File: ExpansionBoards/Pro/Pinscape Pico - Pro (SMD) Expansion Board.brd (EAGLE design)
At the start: 170.6 x 108 mm, 179 parts, among them IC1 UCC27523D, IC10 UCC27523D, IC11 UCC27523D, IC12 UCC27523D, IC13 UCC27523D, IC14 UCC27523D, IC15 TLC59116FIRHBR, IC16 TLC59116FIRHBR, IC17 TLC59116FIRHBR, IC18 TLC59116FIRHBR, IC19 ULN2803ADWR, IC2 UCC27523D, IC20 ULN2803ADWR, IC21 ULN2803ADWR, IC22 ULN2803ADWR, IC23 ULN2803ADWR, IC24 PCA9555APW,118, IC25 PCA9555APW,118, IC26 LIS3DHTR, IC27 SN74LVC1G175DCKR, IC28 APX809S-29SA-7, IC29 LTV-827S, IC3 UCC27523D, IC30 ADS1115IDGSR, IC31 TLV75733PDBVR, IC33 RV-3032-C7, IC4 UCC27523D, IC5 UCC27523D, IC6 UCC27523D, IC7 UCC27523D, IC8 UCC27523D, IC9 UCC27523D, J1 640445-4, J10 1-640456-0, J11 1-640456-0, J12 1-640456-0, J13 640445-5, J14 640445-9, J15 640445-9, J16 640445-9, J18 BM03B-SRSS-TB(LF)(SN), J2 30316-6002HB, J3 1-640456-0, J4 640456-9, J5 640456-9, J6 640454-2, J7 215079-4, J8 30308-6002HB, J9 1-640456-0, Q1 BUK7K89-100EX, Q10 BUK7K89-100EX, Q11 BUK7K89-100EX, Q12 BUK7K89-100EX, Q13 BUK7K89-100EX, Q14 BUK7K89-100EX, Q15 UMA5NTR, Q16 UMA5NTR, Q17 UMA5NTR, Q18 UMA5NTR, Q19 UMA5NTR, Q2 BUK7K89-100EX, Q20 UMA5NTR, Q21 UMA5NTR, Q22 UMA5NTR, Q23 UMA5NTR, Q24 UMA5NTR, Q25 UMA5NTR, Q26 UMA5NTR, Q29 DMG2302UK-7, Q3 BUK7K89-100EX, Q4 BUK7K89-100EX, Q5 BUK7K89-100EX, Q6 BUK7K89-100EX, Q7 BUK7K89-100EX, Q8 BUK7K89-100EX, Q9 BUK7K89-100EX, SW1 TS-1187A-B-A-B, U1 BAT-HLD-001-THM

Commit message: bug fixes
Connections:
- net 3V3_PERIPHERAL: now also IC26.8
- net GND: now also IC26.7; no longer IC26.8
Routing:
- net 3V3_PERIPHERAL: track 399.6 -> 404.9 mm, vias 17 -> 18
- net GND: track 105.4 -> 103.7 mm

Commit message: expansion board improvements
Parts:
- J1: value 640445-4 -> 640445-6; device SamacSys_Parts:SHDR4W117P0X396_1X4_1585X762X1 -> SamacSys_Parts:SHDR6W183P0X396_1X6_2377X762X1
- moved J1 8.71 mm to (157.3, 95.1), turned to 270 degrees
- moved R20 2.10 mm to (97.5, 83.1), turned to 270 degrees
- moved R24 2.06 mm to (114.9, 83.1), turned to 270 degrees
- moved R28 2.06 mm to (132.3, 83.1), turned to 270 degrees
- moved R12 2.06 mm to (62.6, 83.1), turned to 270 degrees
- moved R14 2.06 mm to (71.3, 83.1), turned to 270 degrees
- moved R16 2.06 mm to (80.0, 83.1), turned to 270 degrees
- moved R18 2.06 mm to (88.7, 83.1), turned to 270 degrees
- moved R22 2.06 mm to (106.1, 83.1), turned to 270 degrees
- moved R26 2.02 mm to (123.4, 83.1), turned to 270 degrees
- moved R10 2.02 mm to (53.9, 83.1), turned to 270 degrees
- moved R4 2.01 mm to (24.6, 83.1), turned to 270 degrees
- moved R8 1.99 mm to (45.2, 83.1), turned to 270 degrees
- moved R2 1.97 mm to (15.8, 83.1), turned to 270 degrees
- moved R6 1.97 mm to (36.8, 83.1), turned to 270 degrees
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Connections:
- net 12V: now also J1.5; no longer J1.4
- net 5V: now also J1.6; no longer J1.1
- net GND: now also J1.1, J1.4
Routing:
- net 5V: track 359.3 -> 341.6 mm
- net 12V: track 295.6 -> 290.5 mm
- net N$19: track 5.34 -> 2.07 mm
- net N$9: track 5.30 -> 2.03 mm
- net N$4: track 5.34 -> 2.07 mm
- net N$27: track 5.30 -> 2.03 mm
- net N$16: track 5.34 -> 2.07 mm
- net N$18: track 5.30 -> 2.07 mm
- net N$24: track 5.30 -> 2.07 mm
- net N$11: track 5.30 -> 2.07 mm
- net N$6: track 5.37 -> 2.15 mm
- net N$3: track 5.34 -> 2.14 mm
- net N$33: track 5.20 -> 2.03 mm
- net N$21: track 5.24 -> 2.11 mm
- net N$61: track 5.16 -> 2.03 mm
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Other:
- board text added: "2ND PSU"
- board text added: "REV 20250106"
- board text removed: "REV 20241208"

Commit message: add logo image
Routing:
- net GND: track 103.0 -> 116.7 mm
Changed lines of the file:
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@@
 <via x="138" y="22.9" extent="1-16" drill="0.5"/>
 <via x="138.7" y="9.4" extent="1-16" drill="0.5"/>
-<polygon width="0.2" layer="1" thermals="no">
-<vertex x="155.1" y="92.9"/>
-<vertex x="159.4" y="92.9"/>
-<vertex x="159.4" y="77.3"/>
-<vertex x="155.1" y="77.3"/>
-</polygon>
-<polygon width="0.2" layer="16" thermals="no">
-<vertex x="155" y="92.9"/>
-<vertex x="159.3" y="92.9"/>
-<vertex x="159.3" y="77.3"/>
-<vertex x="155" y="77.3"/>
-</polygon>
 <contactref element="J1" pad="1"/>
+<wire x1="157.3" y1="91.14" x2="155.64" y2="91.14" width="1.5" layer="16"/>
+<wire x1="157.3" y1="87.18" x2="155.78" y2="87.18" width="1.5" layer="16"/>
+<wire x1="157.3" y1="83.22" x2="155.72" y2="83.22" width="1.5" layer="16"/>
+<wire x1="157.3" y1="95.1" x2="155.3" y2="95.1" width="1.5" layer="16"/>
+<wire x1="157.3" y1="95.1" x2="155.3" y2="95.1" width="1.5" layer="1"/>
+<wire x1="157.3" y1="91.14" x2="155.54" y2="91.14" width="1.5" layer="1"/>
+<wire x1="157.3" y1="87.18" x2="155.72" y2="87.18" width="1.5" layer="1"/>
+<wire x1="157.3" y1="83.22" x2="155.62" y2="83.22" width="1.5" layer="1"/>
 </signal>
 <signal name="5V">

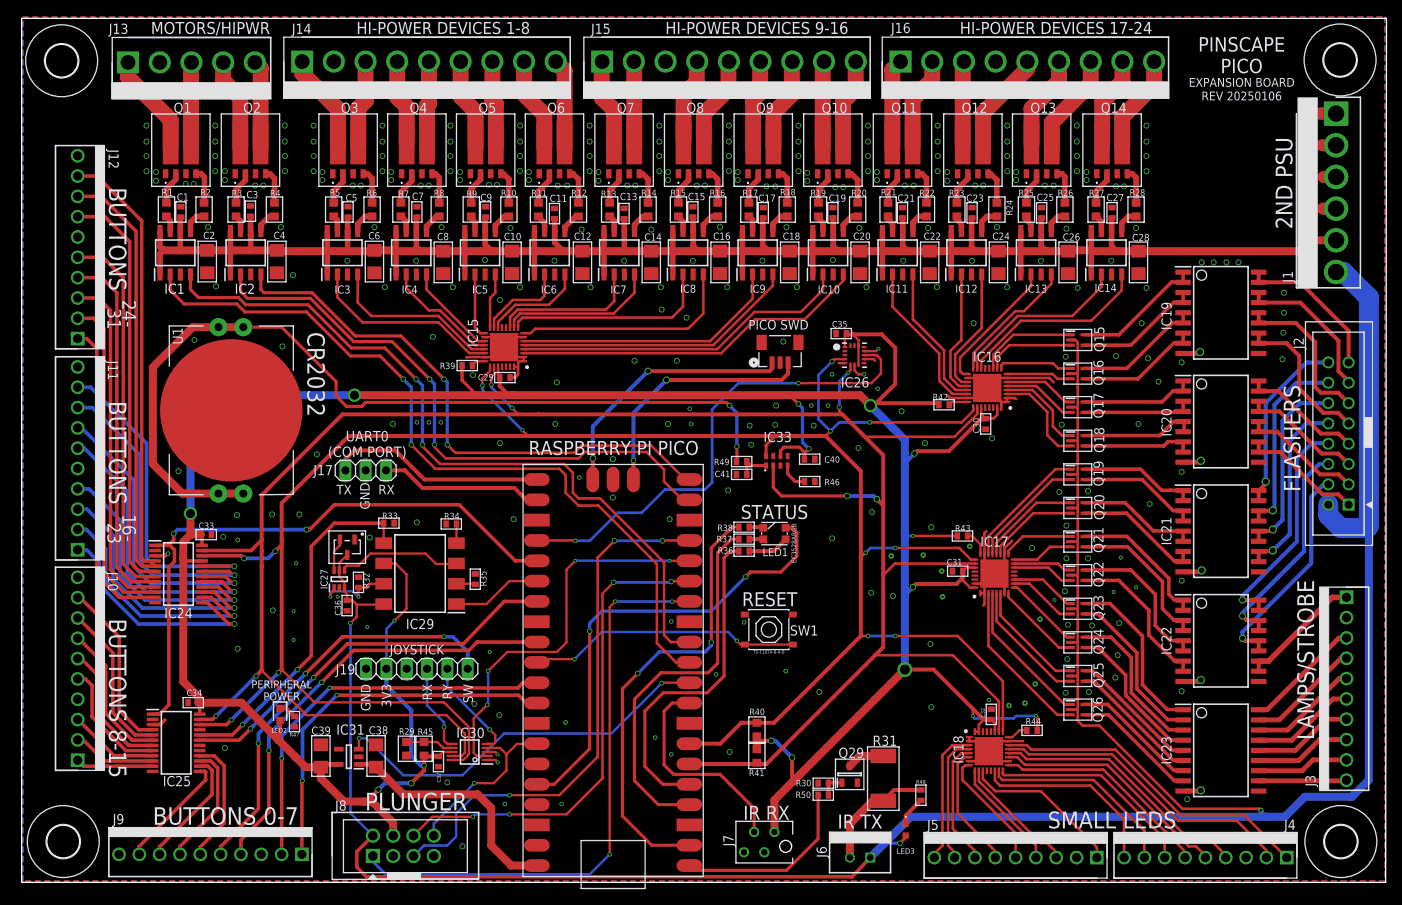
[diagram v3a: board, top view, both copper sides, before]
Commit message: Update Pro expansion board to use 74HC165 for all button inputs
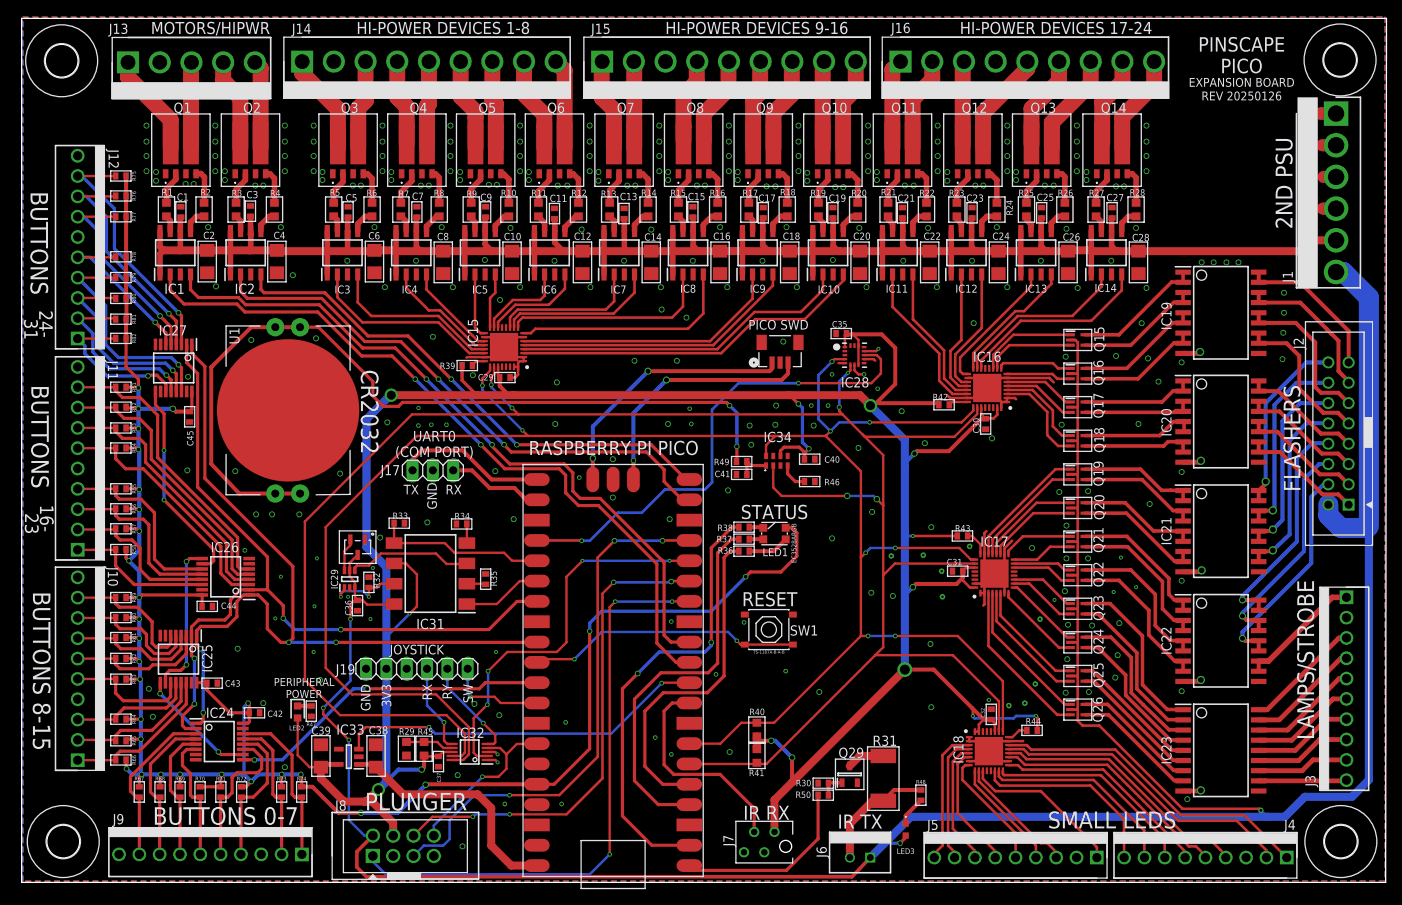
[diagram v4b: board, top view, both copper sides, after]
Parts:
- removed C33, C34: 0.1uF, rcl:C0402
- added C42, C43, C44, C45: 0.1uF, rcl:C0402
- added IC32: ADS1115IDGSR, SamacSys_Parts:SOP50P490X110-10N
- added IC34: RV-3032-C7, SamacSys_Parts:RV3032C7
- added R51, R52, R53, R54, R55, R56, R57, R58, R59, R60, R61, R62, R63, R64, R65, R66, R67, R68, R69, R70, R71, R72, R73, R74, R75, R76, R77, R78, R79, R80, R81, R82: 10k, resistor:R0402
- IC24, IC25: value PCA9555APW,118 -> SN74HC165PWR; device SamacSys_Parts:SOP65P640X110-24N -> SamacSys_Parts:SOP65P640X120-16N
- IC26: value LIS3DHTR -> SN74HC165PWR; device SamacSys_Parts:LIS3DHTR -> SamacSys_Parts:SOP65P640X120-16N
- IC27: value SN74LVC1G175DCKR -> SN74HC165PWR; device SamacSys_Parts:SOP65P210X110-6N -> SamacSys_Parts:SOP65P640X120-16N
- IC28: value APX809S-29SA-7 -> LIS3DHTR; device SamacSys_Parts:SOT23_DIO -> SamacSys_Parts:LIS3DHTR
- IC29: value LTV-827S -> SN74LVC1G175DCKR; device SamacSys_Parts:SOP254P1016X460-8N -> SamacSys_Parts:SOP65P210X110-6N
- IC30: value ADS1115IDGSR -> APX809S-29SA-7; device SamacSys_Parts:SOP50P490X110-10N -> SamacSys_Parts:SOT23_DIO
- IC31: value TLV75733PDBVR -> LTV-827S; device SamacSys_Parts:SOT95P280X145-5N -> SamacSys_Parts:SOP254P1016X460-8N
- IC33: value RV-3032-C7 -> TLV75733PDBVR; device SamacSys_Parts:RV3032C7 -> SamacSys_Parts:SOT95P280X145-5N
- moved IC26 83.3 mm to (18.5, 37.2), turned to 180 degrees
- moved IC28 67.8 mm to (97.1, 64.9), turned to 0 degrees
- moved IC33 65.0 mm to (33.9, 14.7), turned to 180 degrees
- moved IC27 33.5 mm to (12.0, 63.3), turned to 270 degrees
- moved IC30 29.2 mm to (35.0, 40.9)
- moved IC31 25.1 mm to (44.1, 37.6)
- moved IC24 21.6 mm to (17.7, 16.6)
- moved IC25 10.5 mm to (12.6, 26.9), turned to 270 degrees
- moved IC29 8.83 mm to (34.0, 36.9), turned to 90 degrees
- moved J17 8.40 mm to (44.4, 50.5)
- moved U1 7.10 mm to (26.3, 58.0)
- moved R47 2.47 mm to (29.2, 20.4)
- moved LED2 2.22 mm to (27.5, 20.3)
- moved R33 1.30 mm to (40.2, 43.9)
- moved C36 1.30 mm to (35.0, 33.6)
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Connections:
- removed net BUTTON_INTR: IC24.1, IC25.1, PICO1.GP19
- removed net FLIPPER_BTN_1: J9.1, PICO1.GP27_A1
- removed net FLIPPER_BTN_2: J9.2, PICO1.GP26_A0
- removed net FLIPPER_BTN_3: J9.4, PICO1.GP22
- removed net FLIPPER_BTN_4: J9.5, PICO1.GP21
- new net BUTTON1: IC24.14, J9.1, R74.2
- new net BUTTON2: IC24.13, J9.2, R73.2
- new net BUTTON3: IC24.12, J9.4, R72.2
- new net BUTTON32: IC27.3, J12.9, R75.2
- new net BUTTON_CLK: IC24.2, IC25.2, IC26.2, IC27.2, PICO1.GP21
- new net BUTTON_DATA: IC24.9, PICO1.GP26_A0
- new net BUTTON_SHLD: IC24.1, IC25.1, IC26.1, IC27.1, PICO1.GP22
- new net N$78: IC25.10, IC26.9
- new net N$79: IC24.10, IC25.9
- new net N$80: IC26.10, IC27.9
- net 3V3_PERIPHERAL: now also IC28.1, IC28.14, IC28.8, IC31.6, IC32.8, IC33.5, IC34.6; no longer C33.1, C34.1, IC24.21, IC24.24, IC25.24, IC26.1, IC26.14, IC26.8, IC29.6, IC30.8, IC31.5, IC33.6
- net 3V3_PERIPHERAL_ENABLE: now also IC33.3; no longer IC31.3
- net 3V3_PICO: now also C42.1, C43.1, C44.1, C45.1, IC24.16, IC25.16, IC26.16, IC27.16, R51.1, R52.1, R53.1, R54.1, R55.1, R56.1, R57.1, R58.1, R59.1, R60.1, R61.1, R62.1, R63.1, R64.1, R65.1, R66.1, R67.1, R68.1, R69.1, R70.1, R71.1, R72.1, R73.1, R74.1, R75.1, R76.1, R77.1, R78.1, R79.1, R80.1, R81.1, R82.1
- net 5V: now also IC29.3, IC29.5, IC30.3, IC31.8; no longer IC27.3, IC27.5, IC28.3, IC29.8
- net ACCEL_INTR: now also IC28.11; no longer IC26.11
- net ADC_INTR: now also IC32.2; no longer IC30.2
- net BUTTON10: now also IC25.13, J10.2, R65.2; no longer IC25.9, J10.3
- net BUTTON11: now also IC25.12, J10.3, R64.2; no longer IC25.8, J10.5
- net BUTTON12: now also IC25.11, J10.5, R63.2; no longer IC25.7, J10.6
- net BUTTON13: now also IC25.3, J10.6, R62.2; no longer IC25.6, J10.7
- net BUTTON14: now also IC25.4, J10.7, R61.2; no longer IC25.5, J10.8
- net BUTTON15: now also IC25.5, J10.8, R60.2; no longer IC25.4, J10.9
- net BUTTON16: now also IC25.6, J10.9, R59.2; no longer IC24.13, J11.1
- net BUTTON17: now also IC26.14, J11.1, R58.2; no longer IC24.14, J11.2
- net BUTTON18: now also IC26.13, J11.2, R57.2; no longer IC24.15, J11.3
- net BUTTON19: now also IC26.12, J11.3, R56.2; no longer IC24.16, J11.4
- net BUTTON20: now also IC26.11, J11.4, R55.2; no longer IC24.17, J11.6
- net BUTTON21: now also IC26.3, J11.6, R54.2; no longer IC24.18, J11.7
- net BUTTON22: now also IC26.4, J11.7, R53.2; no longer IC24.19, J11.8
- net BUTTON23: now also IC26.5, J11.8, R52.2; no longer IC24.20, J11.9
- net BUTTON24: now also IC26.6, J11.9, R51.2; no longer IC24.11, J12.1
- net BUTTON25: now also IC27.11, J12.1, R82.2; no longer IC24.10, J12.2
- net BUTTON26: now also IC27.12, J12.2, R81.2; no longer IC24.9, J12.3
- net BUTTON27: now also IC27.13, J12.3, R80.2; no longer IC24.8, J12.4
- net BUTTON28: now also IC27.14, J12.4, R79.2; no longer IC24.7, J12.5
- net BUTTON29: now also IC27.6, J12.5, R78.2; no longer IC24.6, J12.7
- net BUTTON30: now also IC27.5, J12.7, R77.2; no longer IC24.5, J12.8
- net BUTTON31: now also IC27.4, J12.8, R76.2; no longer IC24.4, J12.9
- net BUTTON4: now also IC24.11, J9.5, R71.2; no longer IC25.16, J9.6
- net BUTTON5: now also IC24.6, J9.6, R70.2; no longer IC25.15, J9.7
- net BUTTON6: now also IC24.5, J9.7, R69.2; no longer IC25.14, J9.8
- net BUTTON7: now also IC24.4, J9.8, R68.2; no longer IC25.13, J9.9
- net BUTTON8: now also IC24.3, J9.9, R67.2; no longer IC25.11, J10.1
- net BUTTON9: now also IC25.14, J10.1, R66.2; no longer IC25.10, J10.2
- net GND: now also C42.2, C43.2, C44.2, C45.2, IC24.15, IC24.8, IC25.15, IC25.8, IC26.15, IC26.8, IC27.15, IC27.8, IC28.10, IC28.12, IC28.5, IC28.7, IC29.2, IC32.1, IC32.3, IC33.2, IC34.5; no longer C33.2, C34.2, IC24.12, IC24.2, IC24.3, IC25.12, IC25.2, IC25.21, IC25.3, IC26.10, IC26.12, IC26.5, IC26.7, IC27.2, IC28.1, IC30.3, IC31.2, IC33.5
- net JOYSTICK_BUTTON: now also PICO1.GP27_A1; no longer IC25.19
- net JOYSTICK_X: now also IC32.6; no longer IC30.6
- net JOYSTICK_Y: now also IC32.5; no longer IC30.5
- net N$58: now also IC29.1, IC31.7; no longer IC27.1, IC29.7
- net N$59: now also IC31.2; no longer IC29.2
- net N$63: now also IC29.6, IC30.2; no longer IC27.6, IC28.2
- net N$65: now also IC31.4; no longer IC29.4
- net N$68: now also IC29.4, IC31.3; no longer IC27.4, IC29.3
- net N$71: now also IC32.7; no longer IC30.7
- net N$73: now also IC34.4; no longer IC33.4
- net N$76: now also IC34.1; no longer IC33.1
- net PLUNGER_ADC: now also IC32.4; no longer IC30.4
- net PSU2_STATUS_SENSE: now also IC31.5, PICO1.GP19; no longer IC25.20, IC29.5
- net PSU2_STATUS_SET: now also IC31.1; no longer IC29.1
- net SCL: now also IC28.4, IC32.10, IC34.8; no longer IC24.22, IC25.22, IC26.4, IC30.10, IC33.8
- net SDA: now also IC28.6, IC32.9, IC34.2; no longer IC24.23, IC25.23, IC26.6, IC30.9, IC33.2
- net VBUS: now also IC33.1; no longer IC31.1
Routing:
- net 3V3_PICO: track 58.1 -> 269.8 mm, vias 2 -> 29
- net BUTTON_SHLD: track 0.00 -> 105.1 mm, vias 0 -> 4
- net BUTTON_CLK: track 0.00 -> 100.4 mm, vias 0 -> 4
- net BUTTON_INTR: track 76.4 -> 0.00 mm, vias 2 -> 0
- net FLIPPER_BTN_4: track 58.8 -> 0.00 mm, vias 2 -> 0
- net FLIPPER_BTN_3: track 54.7 -> 0.00 mm, vias 2 -> 0
- net FLIPPER_BTN_2: track 49.5 -> 0.00 mm, vias 2 -> 0
- net FLIPPER_BTN_1: track 47.1 -> 0.00 mm, vias 2 -> 0
- net 3V3_PERIPHERAL: track 403.3 -> 359.3 mm, vias 17 -> 15
- net SCL: track 294.8 -> 253.6 mm, vias 13 -> 9
- net BUTTON_DATA: track 0.00 -> 40.8 mm, vias 0 -> 2
- net SDA: track 298.7 -> 263.2 mm, vias 8 -> 6
- net BUTTON32: track 0.00 -> 31.5 mm, vias 0 -> 1
- net BUTTON29: track 51.5 -> 21.2 mm, vias 0 -> 1
- net JOYSTICK_BUTTON: track 41.8 -> 12.3 mm, vias 3 -> 1
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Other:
- board text added: "REV 20250126"
- board text removed: "REV 20250106"

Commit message: change to socketed Pico for Pro board
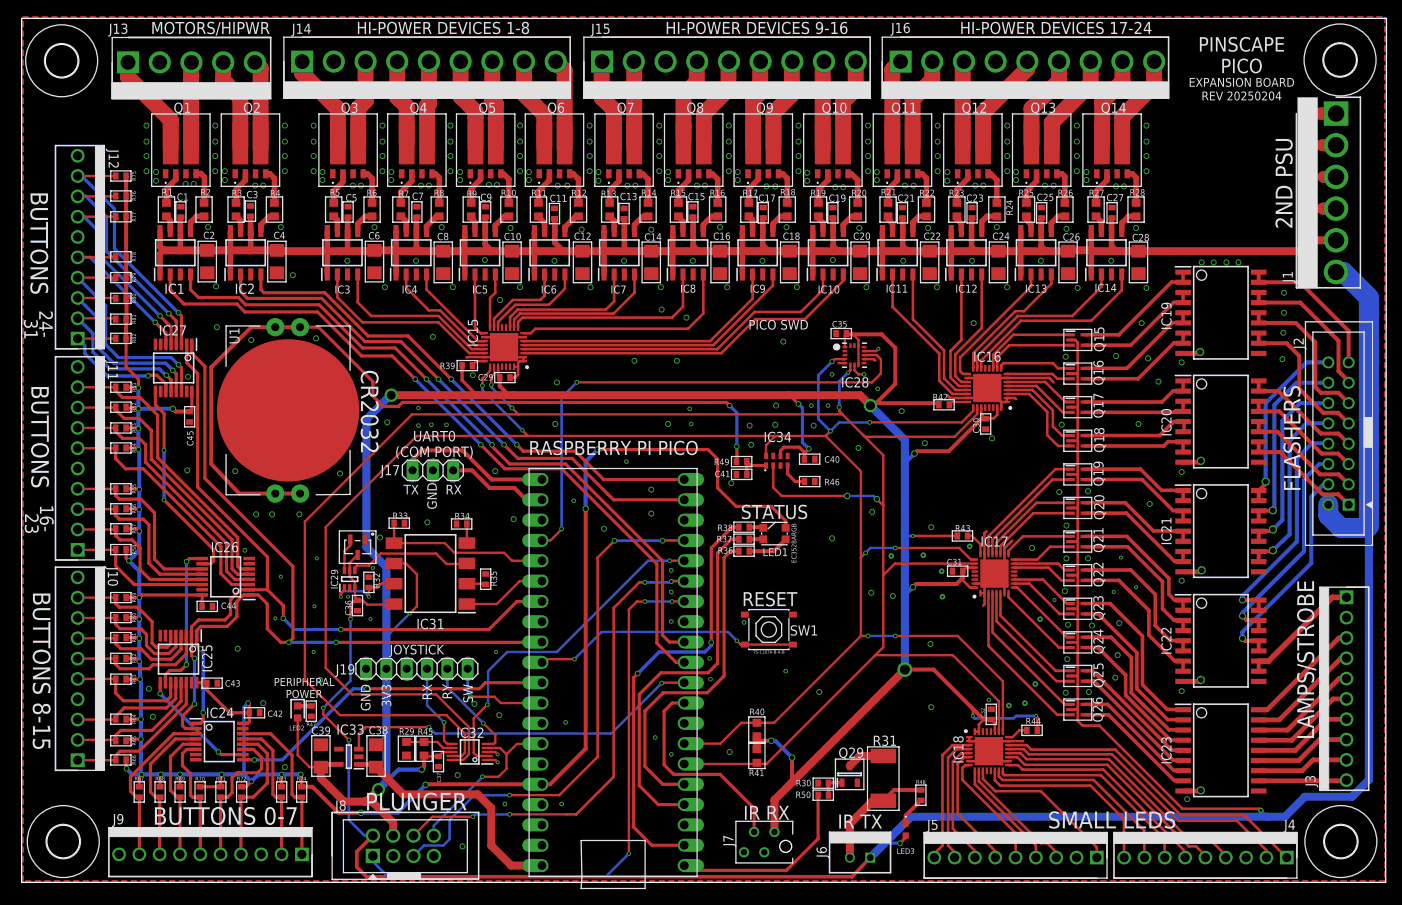
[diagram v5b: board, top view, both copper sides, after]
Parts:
- removed J18: BM03B-SRSS-TB(LF)(SN), SamacSys_Parts:CONN_BM03B-SRSS-TB(LF)(SN)_JST
- PICO1: device RaspberryPi_Pico:RPI_PICO -> RaspberryPi_Pico:RPI_PICO_TH_NO_DEBUG
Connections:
- removed net SWCLK: J18.3, PICO1.SWCLK
- removed net SWDIO: J18.1, PICO1.SWDIO
- net GND: no longer J18.2, PICO1.GND@5
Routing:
- net SWDIO: track 32.8 -> 0.00 mm, vias 2 -> 0
- net SWCLK: track 31.1 -> 0.00 mm, vias 2 -> 0
- net 3V3_PICO: track 269.8 -> 287.8 mm
- net ADC_INTR: track 50.0 -> 44.9 mm, vias 4 -> 2
- net ACCEL_INTR: track 61.1 -> 64.7 mm
- net /MOTORCTL1: track 93.2 -> 91.3 mm
- net /MOTORCTL2: track 89.3 -> 87.4 mm
- net PLUNGER_IRQ1_SCL: track 61.2 -> 59.4 mm
- net LED_R: track 55.8 -> 54.0 mm
- net /MOTORCTL3: track 69.9 -> 68.6 mm
- net PLUNGER_ADC: track 23.7 -> 24.9 mm
- net LED_G: track 47.8 -> 46.7 mm
- net /MOTORCTL4: track 65.3 -> 64.6 mm
- net N$70: track 34.2 -> 33.6 mm
- net SCL: track 253.6 -> 254.3 mm
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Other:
- board text added: "REV 20250204"
- board text removed: "REV 20250126"

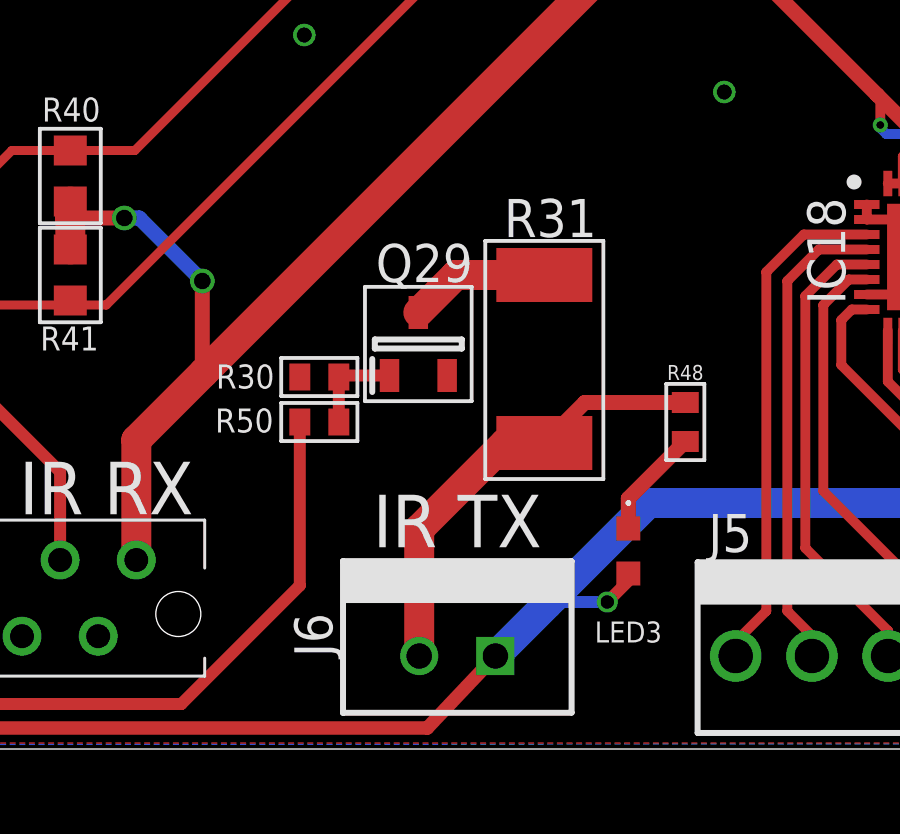
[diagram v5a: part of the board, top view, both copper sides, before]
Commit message: add tlc59116 wiring diagram to json doc; change Pro board IRED to constant-current circuit
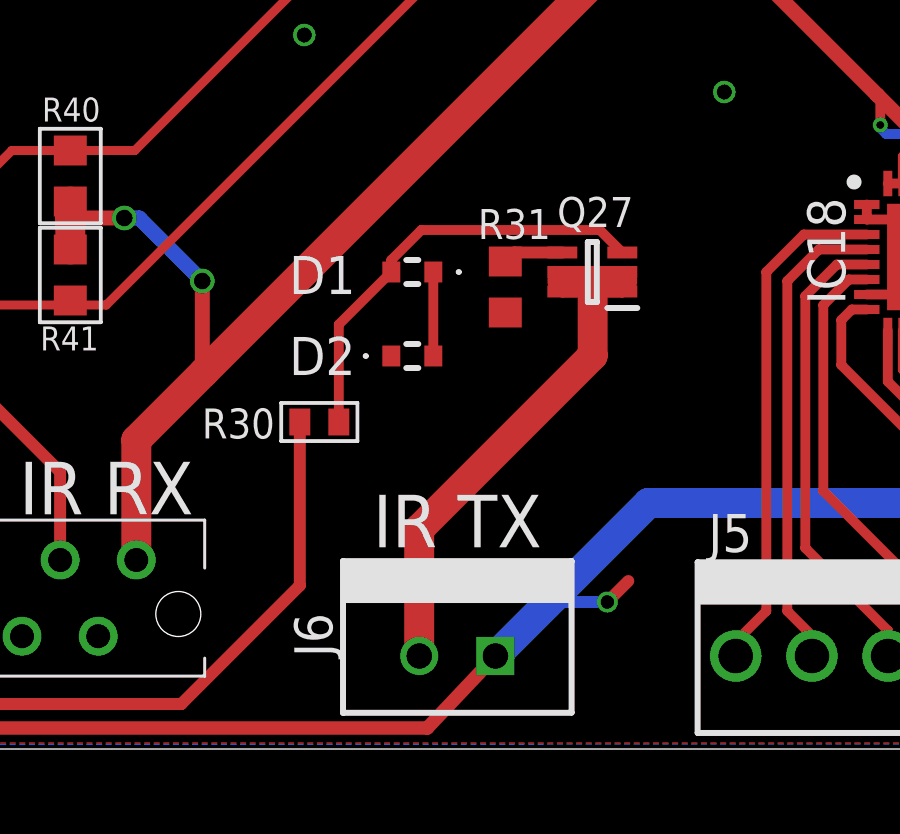
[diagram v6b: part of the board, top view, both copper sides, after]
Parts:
- removed LED3: LS_L29K-G1J2-1, SamacSys_Parts:LSL29KG1J21
- removed Q29: DMG2302UK-7, SamacSys_Parts:SOT96P240X110-3N
- removed R48: 1.6K, resistor:R0402
- removed R50: 330R, resistor:R0402
- added D1, D2: 1N4148WT-7, SamacSys_Parts:1N4148WT7
- added Q27: DSS8110Y-7, SamacSys_Parts:SOT65P210X110-6N
- R30: value 10K -> 540R
- R31: value 3R 1W -> 2R5; device rcl:R2512 -> rcl:R0603
- moved R31 2.73 mm to (99.4, 14.4), turned to 90 degrees
- moved R30 1.50 mm to (93.2, 9.90), turned to 180 degrees
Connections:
- removed net N$75: LED3.1, R48.2
- new net N$81: D1.1, D2.2
- net 5V: no longer LED3.2
- net GND: now also D2.1, R31.1; no longer Q29.2, R30.1
- net IR_LED_CATHODE: now also Q27.1, Q27.2, Q27.5, Q27.6; no longer R31.2, R48.1
- net IR_OUT: now also R30.2; no longer R50.2
- net N$32: now also Q27.4, R31.2; no longer Q29.3, R31.1
- net N$77: now also D1.2, Q27.3, R30.1; no longer Q29.1, R30.2, R50.1
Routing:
- net N$77: track 3.21 -> 14.5 mm
- net IR_LED_CATHODE: track 14.8 -> 21.8 mm
- net N$75: track 3.69 -> 0.00 mm
- net N$81: track 0.00 -> 2.80 mm
- net N$32: track 4.72 -> 2.02 mm
